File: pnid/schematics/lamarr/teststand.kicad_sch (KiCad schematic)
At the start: 68 parts

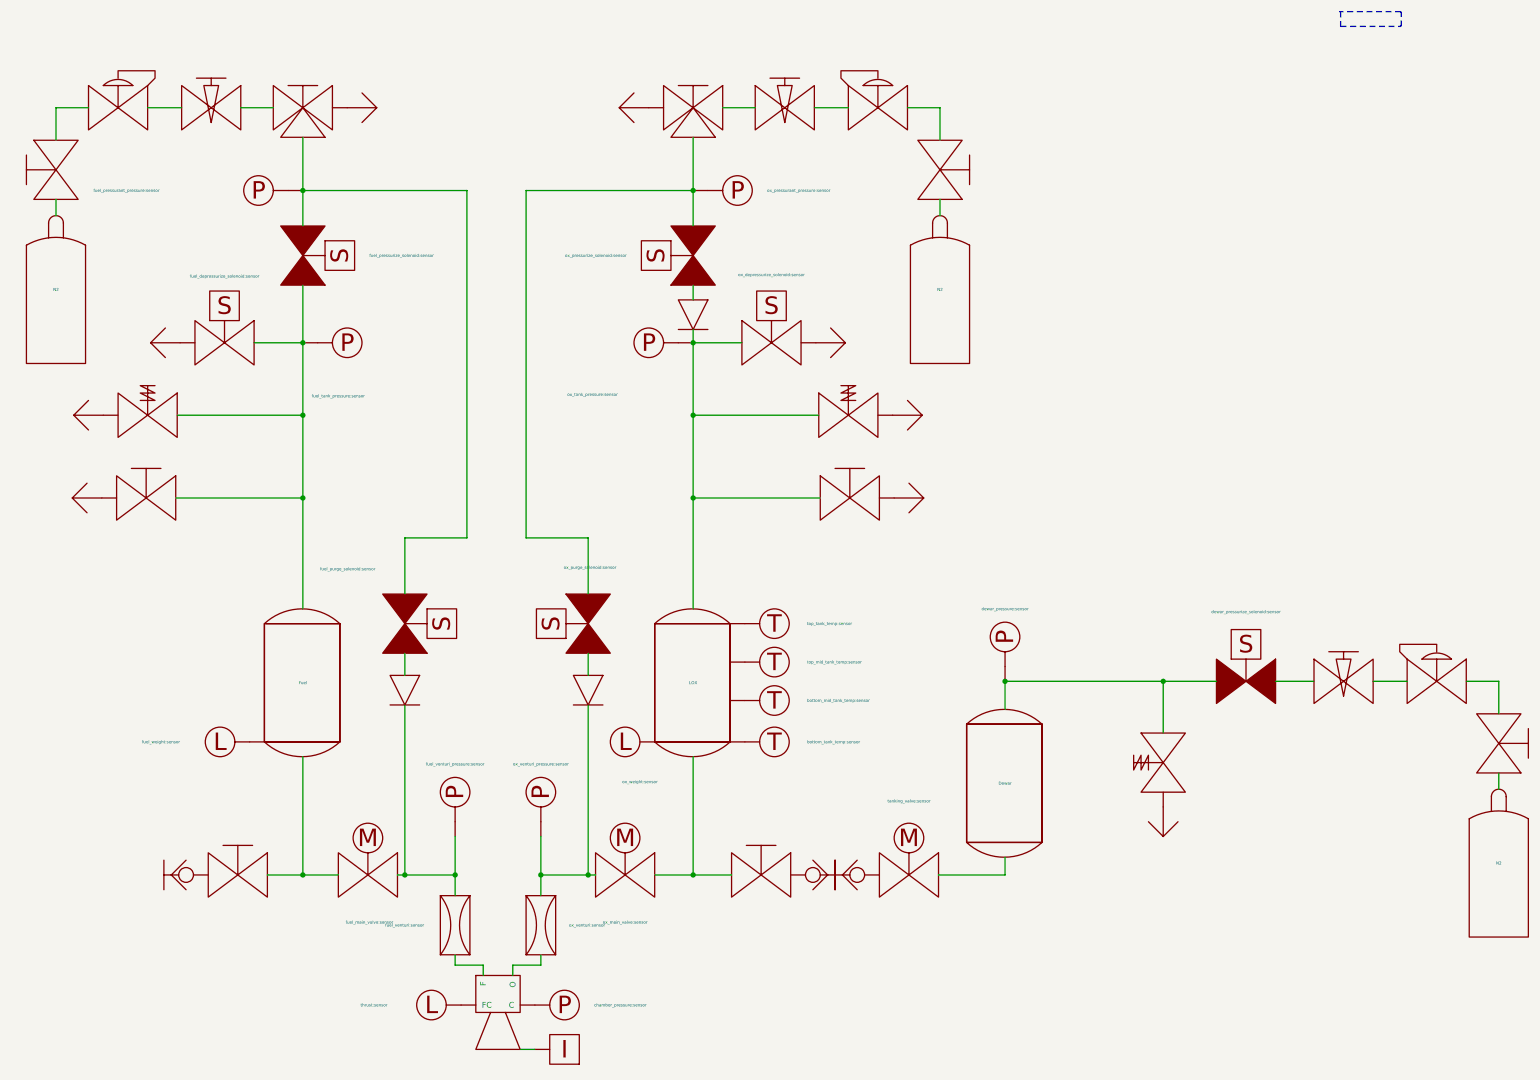
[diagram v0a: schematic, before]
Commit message: update to kicad 8 and fix migration issues
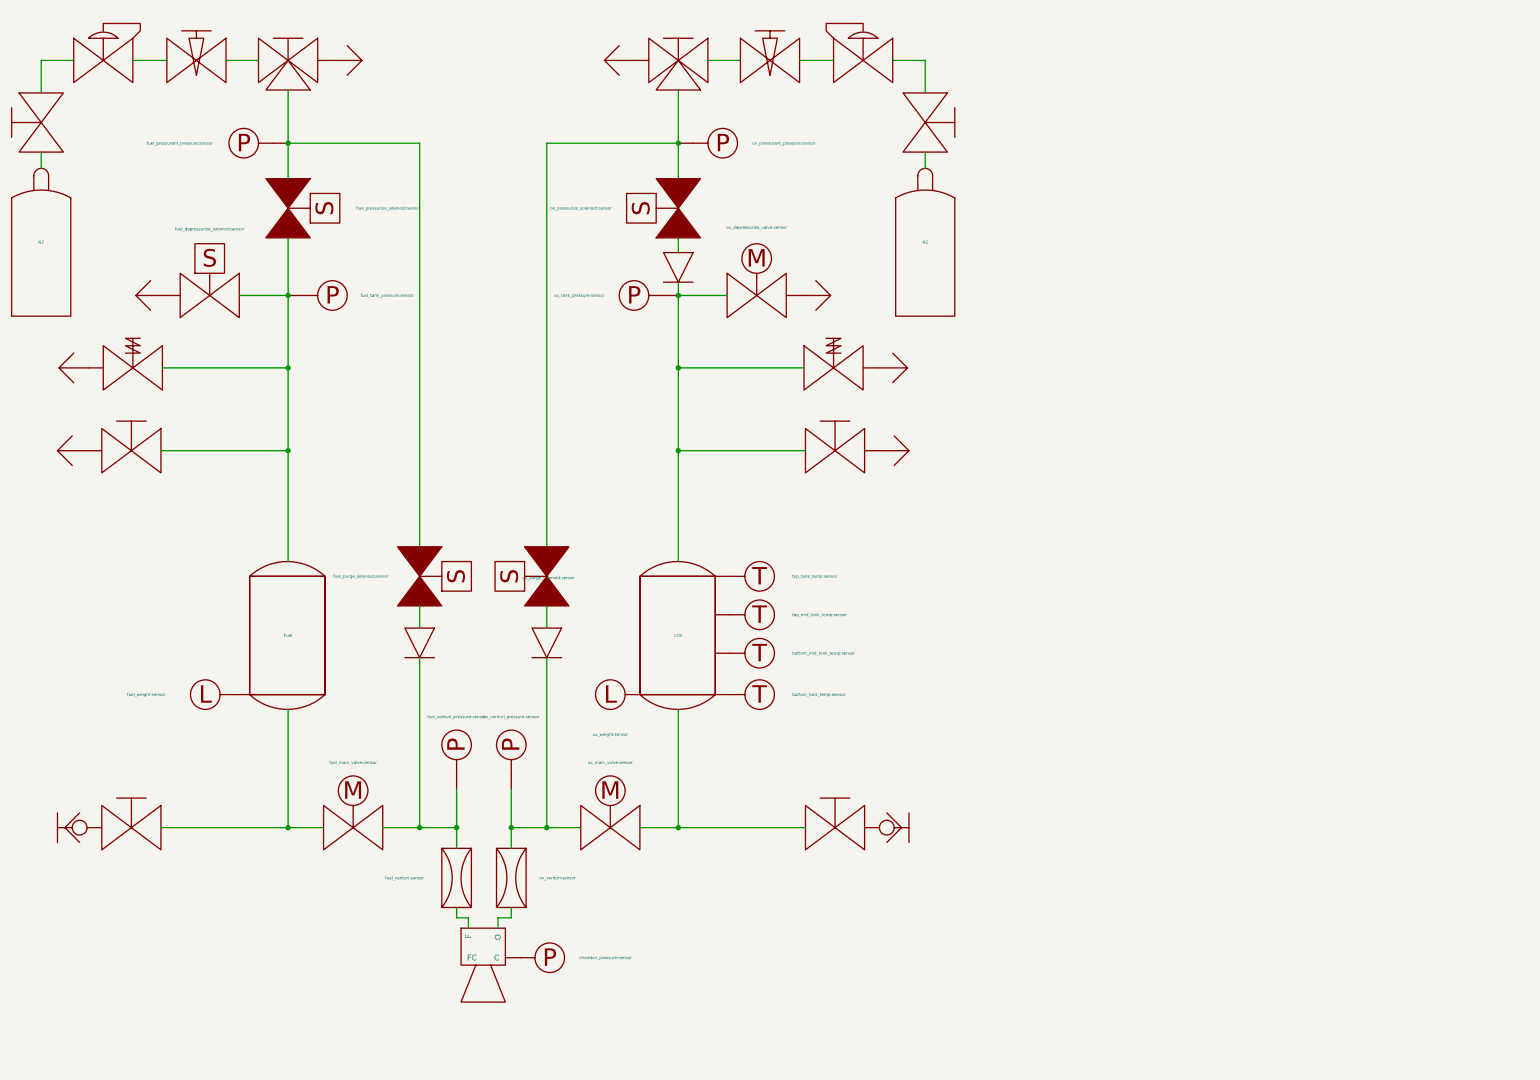
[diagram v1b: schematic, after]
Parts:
- removed Dewar: dewar_fill_level:sensor, symbol lamarr-rescue:Tank_Slim-PnID-Lib
- removed DewarOverPressureValve?: DewarOverPressureValve, symbol lamarr-rescue:Valve_OverPressure-PnID-Lib
- removed DewarQuickConnect?: DewarQuickConnect, symbol lamarr-rescue:QuickConnect_Half-PnID-Lib
- removed N2 (x2): N2, symbol lamarr-rescue:GasBottle-PnID-Lib
- removed Vent? (x2): Vent, symbol lamarr-rescue:Vent-PnID-Lib
- removed dewar_manual_valve?: dewar_manual_valve, symbol lamarr-rescue:Valve_Manual-PnID-Lib
- removed dewar_needle_valve?: dewar_needle_valve, symbol lamarr-rescue:Valve_Needle-PnID-Lib
- removed dewar_pressure?: dewar_pressure:sensor, symbol lamarr-rescue:Sensor_Pressure-PnID-Lib
- removed dewar_pressure_regulator?: dewar_pressure_regulator, symbol lamarr-rescue:PressureRegulator-PnID-Lib
- removed dewar_pressurize_solenoid?: dewar_pressurize_solenoid:sensor, symbol lamarr-rescue:Valve_Solenoid_NC-PnID-Lib
- removed fuel_weight: fuel_weight:sensor, symbol lamarr-rescue:Sensor_Load-PnID-Lib
- removed igniter: igniter:sensor, symbol lamarr-rescue:igniter-PnID-Lib
- removed ox_manual_valve?: ox_manual_valve, symbol lamarr-rescue:Valve_Manual-PnID-Lib
- removed ox_weight: ox_weight:sensor, symbol lamarr-rescue:Sensor_Load_Short-PnID-Lib
- removed tanking_valve?: tanking_valve:sensor, symbol lamarr-rescue:Valve_Servo-PnID-Lib
- removed thrust: thrust:sensor, symbol lamarr-rescue:Sensor_Load-PnID-Lib
- added N2: N2, symbol PnID-Lib:GasBottle
- added Vent?: Vent, symbol PnID-Lib:Vent
- added fuel_weight: fuel_weight:sensor, symbol teststand-rescue:Sensor_Load-PnID-Lib
- added ox_manual_valve: ox_manual_valve, symbol PnID-Lib:Valve_Manual
- added ox_weight: ox_weight:sensor, symbol PnID-Lib:Sensor_Load_Short
- CheckValve? (x3): symbol lamarr-rescue:CheckValve-PnID-Lib -> PnID-Lib:CheckValve
- Fuel, LOX: symbol lamarr-rescue:Tank_Slim-PnID-Lib -> PnID-Lib:Tank_Slim
- N2: symbol lamarr-rescue:GasBottle-PnID-Lib -> PnID-Lib:GasBottle
- Vent? (x7): symbol lamarr-rescue:Vent-PnID-Lib -> PnID-Lib:Vent
- bottom_mid_tank_temp, bottom_tank_temp, top_mid_tank_temp, top_tank_temp: symbol lamarr-rescue:Sensor_Temperature-PnID-Lib -> PnID-Lib:Sensor_Temperature
- chamber_pressure, fuel_pressurant_pressure, fuel_tank_pressure, fuel_venturi_pressure, ox_pressurant_pressure:sensor, ox_tank_pressure, ox_venturi_pressure: symbol lamarr-rescue:Sensor_Pressure-PnID-Lib -> PnID-Lib:Sensor_Pressure
- engine: symbol lamarr-rescue:Engine-PnID-Lib -> PnID-Lib:Engine
- fuel_depressurize_solenoid: symbol lamarr-rescue:Valve_Solenoid_NO-PnID-Lib -> PnID-Lib:Valve_Solenoid_NO
- fuel_main_valve, ox_main_valve: symbol lamarr-rescue:Valve_Servo-PnID-Lib -> PnID-Lib:Valve_Servo
- fuel_manual_3way, fuel_manual_3way?: symbol lamarr-rescue:Valve_Manual_3Way-PnID-Lib -> teststand-rescue:Valve_Manual_3Way-PnID-Lib
- fuel_manual_tanking_valve, fuel_manual_valve, fuel_manual_vent_valve, ox_manual_tanking_valve, ox_manual_vent_valve: symbol lamarr-rescue:Valve_Manual-PnID-Lib -> PnID-Lib:Valve_Manual
- fuel_needle_valve, ox_needle_valve: symbol lamarr-rescue:Valve_Needle-PnID-Lib -> PnID-Lib:Valve_Needle
- fuel_pressure_regulator, ox_pressure_regulator: symbol lamarr-rescue:PressureRegulator-PnID-Lib -> PnID-Lib:PressureRegulator
- fuel_pressurize_solenoid, fuel_purge_solenoid, ox_pressurize_solenoid, ox_purge_solenoid: symbol lamarr-rescue:Valve_Solenoid_NC-PnID-Lib -> PnID-Lib:Valve_Solenoid_NC
- fuel_quick_connect, ox_quick_connect: symbol lamarr-rescue:QuickConnect_Half-PnID-Lib -> PnID-Lib:QuickConnect_Half
- fuel_safety_valve, ox_safety_valve: symbol lamarr-rescue:Valve_OverPressure-PnID-Lib -> PnID-Lib:Valve_OverPressure
- fuel_venturi, ox_venturi: symbol lamarr-rescue:Venturi-PnID-Lib -> PnID-Lib:Venturi
- ox_depressurize_valve: renamed from ox_depressurize_solenoid; value ox_depressurize_solenoid:sensor -> ox_depressurize_valve:sensor; symbol lamarr-rescue:Valve_Solenoid_NO-PnID-Lib -> PnID-Lib:Valve_Servo
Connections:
- net at engine.~ (O): now also fuel_venturi.~; no longer ox_venturi.~
- net at fuel_venturi.~: now also CheckValve?.~, fuel_main_valve.~, fuel_venturi_pressure.~; no longer engine.~ (O)
- net at ox_manual_vent_valve.~: now also Vent?.~
- net at ox_pressure_regulator.~: now also ox_manual_valve.~; no longer ox_needle_valve.~
- new net: fuel_manual_3way?.~, ox_pressurant_pressure:sensor.~, ox_pressurize_solenoid.~, ox_purge_solenoid.~
- new net: fuel_manual_3way.~, fuel_pressurant_pressure.~, fuel_pressurize_solenoid.~, fuel_purge_solenoid.~
- new net: Fuel.~, fuel_depressurize_solenoid.~, fuel_manual_vent_valve.~, fuel_pressurize_solenoid.~, fuel_safety_valve.~, fuel_tank_pressure.~
- new net: CheckValve?.~, LOX.~, ox_depressurize_valve.~, ox_manual_vent_valve.~, ox_safety_valve.~, ox_tank_pressure.~
- new net: LOX.~, ox_main_valve.~, ox_manual_tanking_valve.~
- new net: Fuel.~, fuel_main_valve.~, fuel_manual_tanking_valve.~
- new net: engine.~ (O), ox_venturi.~
- new net: ox_needle_valve.~, ox_pressure_regulator.~
- new net: N2.~, ox_manual_valve.~
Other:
- moved on the sheet: Fuel, LOX, N2
